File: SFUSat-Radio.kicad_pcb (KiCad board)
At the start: 2 copper layers, 95.9 x 90.2 mm, 84 parts, among them J1 PC104-8BIT, J2 PC104PTH, J3 PC104PTH, J4 PC104PTH, J5 PC104PTH, J6 SMA, J7 SMA, J8 SMA, J9 SMA, P1 CONN_02X05, P2 CONN_01X03, P3 CONN_01X03, P4 CONN_01X03, U1 2N7002DW, U10 RT9183, U2 CC1101-Q1, U3 0433BM15A0001, U4 SINGLE_0402, U5 SKY13372-467LF, U6 SINGLE_0402, U7 SINGLE_0402, U8 SKY65366-21, U9 TPS799, X1 NX3225GA

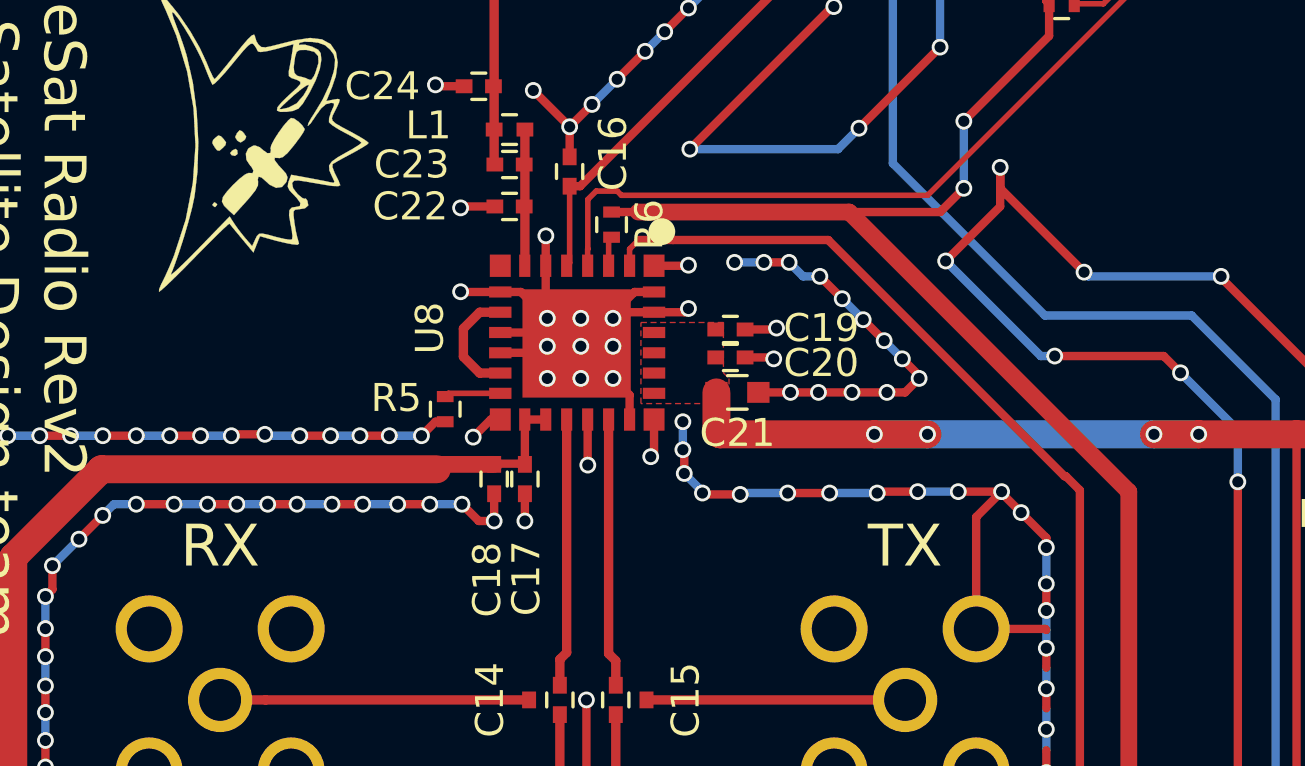
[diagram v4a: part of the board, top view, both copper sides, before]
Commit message: IC->passive pad 30mil clearance
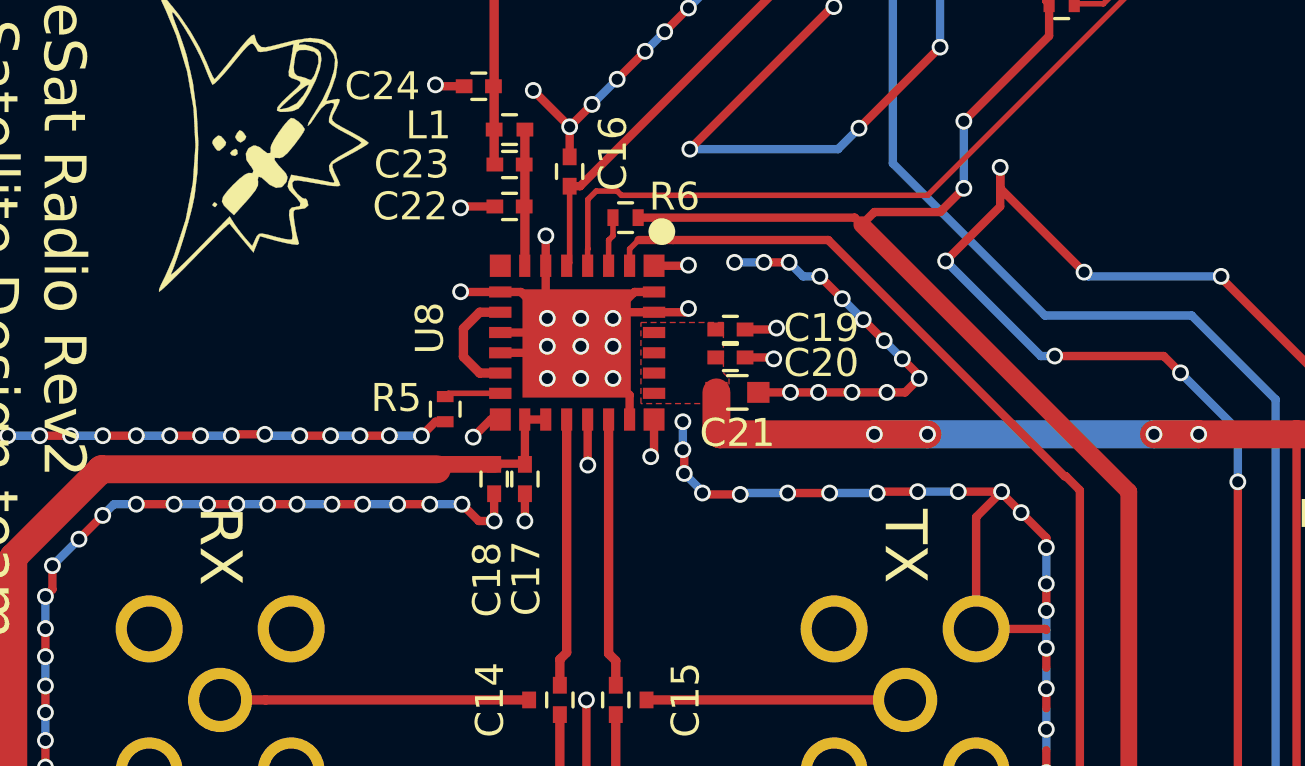
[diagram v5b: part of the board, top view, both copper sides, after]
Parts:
- moved R6 0.56 mm to (140.5, 85.8), turned to 180 degrees
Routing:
- net /VDD_3.3: track 299.1 -> 297.9 mm
- net Net-(R6-Pad2): track 1.06 -> 1.78 mm
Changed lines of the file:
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@@
     (thickness 1.6)
     (drawings 27)
-    (tracks 1250)
+    (tracks 1252)
     (zones 0)
     (modules 84)
@@
   )
   (module SFUSat:R_0402 (layer F.Cu)
-    (at 140 86 270)
+    (at 140.5 85.75 180)
     (descr "Resistor SMD 0402, reflow soldering, Vishay (see dcrcw.pdf)")
     (tags "resistor 0402")
     (attr smd)
-    (fp_text reference R6 (at 0 -1.35 270) (layer F.SilkS)
+    (fp_text reference R6 (at -1.75 0.75 180) (layer F.SilkS)
       (effects (font (size 1 1) (thickness 0.15)))
     )
-    (fp_text value 1k (at 0 1.45 270) (layer F.Fab)
+    (fp_text value 1k (at 0 1.45 180) (layer F.Fab)
       (effects (font (size 1 1) (thickness 0.15)))
     )
-    (fp_text user %R (at 0 -1.35 270) (layer F.Fab)
+    (fp_text user %R (at 0 -1.35 180) (layer F.Fab)
       (effects (font (size 1 1) (thickness 0.15)))
     )
@@
     (fp_line (start 0.8 0.45) (end 0.8 -0.45) (layer F.CrtYd) (width 0.05))
     (fp_line (start 0.8 0.45) (end -0.8 0.45) (layer F.CrtYd) (width 0.05))
-    (pad 1 smd rect (at -0.45 0 270) (size 0.4 0.6) (layers F.Cu F.Paste F.Mask)
+    (pad 1 smd rect (at -0.45 0 180) (size 0.4 0.6) (layers F.Cu F.Paste F.Mask)
       (net 4 /VDD_3.3) (solder_paste_margin -0.02))
-    (pad 2 smd rect (at 0.45 0 270) (size 0.4 0.6) (layers F.Cu F.Paste F.Mask)
+    (pad 2 smd rect (at 0.45 0 180) (size 0.4 0.6) (layers F.Cu F.Paste F.Mask)
       (net 89 "Net-(R6-Pad2)") (solder_paste_margin -0.02))
     (model Resistors_SMD.3dshapes/R_0402.wrl
@@
     (effects (font (size 1.5 1.5) (thickness 0.3)))
   )
-  (gr_text TX (at 150.5 97.5) (layer F.SilkS)
+  (gr_text TX (at 150.5 97.5 270) (layer F.SilkS)
     (effects (font (size 1.5 1.5) (thickness 0.3)))
   )
-  (gr_text RX (at 126 97.5) (layer F.SilkS)
+  (gr_text RX (at 126 97.5 270) (layer F.SilkS)
     (effects (font (size 1.5 1.5) (thickness 0.3)))
   )
@@
   (segment (start 150 126.95) (end 150 125.45) (width 0.2) (layer F.Cu) (net 3))
   (segment (start 150 125.45) (end 149.95 125.4) (width 0.2) (layer F.Cu) (net 3))
+  (segment (start 151.75 85.55) (end 149.398542 85.55) (width 0.3) (layer F.Cu) (net 4))
+  (segment (start 149.398542 85.55) (end 148.948542 86) (width 0.3) (layer F.Cu) (net 4))
+  (segment (start 148.948542 86) (end 158.5 95.551458) (width 0.6) (layer F.Cu) (net 4))
+  (segment (start 148.698542 85.75) (end 148.948542 86) (width 0.3) (layer F.Cu) (net 4))
+  (segment (start 140.95 85.75) (end 148.698542 85.75) (width 0.3) (layer F.Cu) (net 4))
   (segment (start 176.399999 146.100001) (end 170.35 146.100001) (width 0.3) (layer F.Cu) (net 4))
   (segment (start 170.35 146.100001) (end 168.9 146.100001) (width 0.3) (layer F.Cu) (net 4))
@@
   (via (at 152.6 82.3) (size 0.6) (drill 0.4) (layers F.Cu B.Cu) (net 4))
   (segment (start 152.6 84.7) (end 152.6 82.3) (width 0.3) (layer B.Cu) (net 4))
-  (segment (start 148.498542 85.55) (end 151.75 85.55) (width 0.3) (layer F.Cu) (net 4))
   (segment (start 151.75 85.55) (end 152.6 84.7) (width 0.3) (layer F.Cu) (net 4))
   (via (at 152.6 84.7) (size 0.6) (drill 0.4) (layers F.Cu B.Cu) (net 4))
@@
   (segment (start 158.5 125.948542) (end 158.5 115.8) (width 0.6) (layer F.Cu) (net 4))
   (segment (start 158.5 115.8) (end 158.5 116.2) (width 0.6) (layer F.Cu) (net 4))
-  (segment (start 140.95 85.55) (end 148.498542 85.55) (width 0.6) (layer F.Cu) (net 4))
-  (segment (start 148.498542 85.55) (end 158.5 95.551458) (width 0.6) (layer F.Cu) (net 4))
   (segment (start 145.15 127.4) (end 145.15 127.45) (width 0.3) (layer F.Cu) (net 4))
   (segment (start 143.7 125.25) (end 143.7 125.36261) (width 0.3) (layer F.Cu) (net 4))
@@
   (segment (start 136.9 94.55) (end 136.9 92.976) (width 0.3) (layer F.Cu) (net 4))
   (segment (start 136.9 92.976) (end 136.8945 92.9705) (width 0.3) (layer F.Cu) (net 4))
-  (segment (start 140 85.55) (end 140.95 85.55) (width 0.3) (layer F.Cu) (net 4))
   (segment (start 142.875 130) (end 144.288001 129.999999) (width 0.2) (layer F.Cu) (net 5))
   (segment (start 144.288001 129.999999) (end 144.600001 130.311999) (width 0.2) (layer F.Cu) (net 5))
@@
   (segment (start 136.0195 92.0335) (end 134.1665 92.0335) (width 0.2) (layer F.Cu) (net 88))
   (segment (start 134.1665 92.0335) (end 134.05 92.15) (width 0.2) (layer F.Cu) (net 88))
-  (segment (start 139.8945 87.4705) (end 139.8945 86.5555) (width 0.2) (layer F.Cu) (net 89))
-  (segment (start 139.8945 86.5555) (end 140 86.45) (width 0.2) (layer F.Cu) (net 89))
+  (segment (start 140.05 85.75) (end 140.05 86.4) (width 0.2) (layer F.Cu) (net 89))
+  (segment (start 140.05 86.4) (end 139.8945 86.5555) (width 0.2) (layer F.Cu) (net 89))
+  (segment (start 139.8945 86.5555) (end 139.8945 87.4705) (width 0.2) (layer F.Cu) (net 89))
   (segment (start 176.566726 96.321568) (end 176.566726 99.324568) (width 0.2) (layer F.Cu) (net 90))
   (segment (start 176.566726 99.324568) (end 177.009726 99.767568) (width 0.2) (layer F.Cu) (net 90))

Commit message: generated gerbers
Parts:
- removed C18: 220pF, SFUSat:C_0402
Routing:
- net GND: track 682.4 -> 655.8 mm, vias 288 -> 266
- net (no net): track 22.2 -> 47.7 mm, vias 15 -> 42

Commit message: added PCBway info
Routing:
- net (no net): track 47.7 -> 0.00 mm, vias 42 -> 0
- net GND: track 655.8 -> 699.4 mm, vias 266 -> 316
- net Net-(C22-Pad1): track 4.88 -> 5.90 mm
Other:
- net class RF: trace_width 0.335589 -> 1.05758

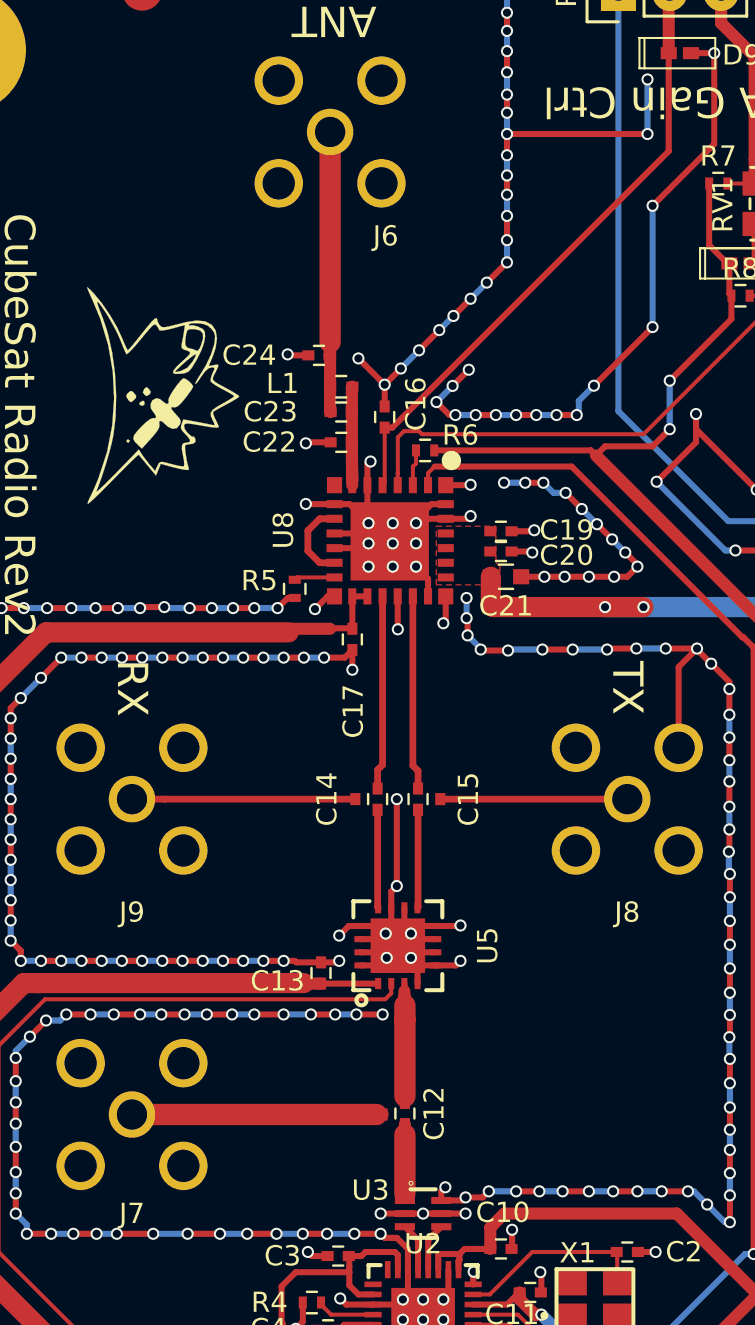
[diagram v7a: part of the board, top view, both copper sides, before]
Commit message: fixed microstrip
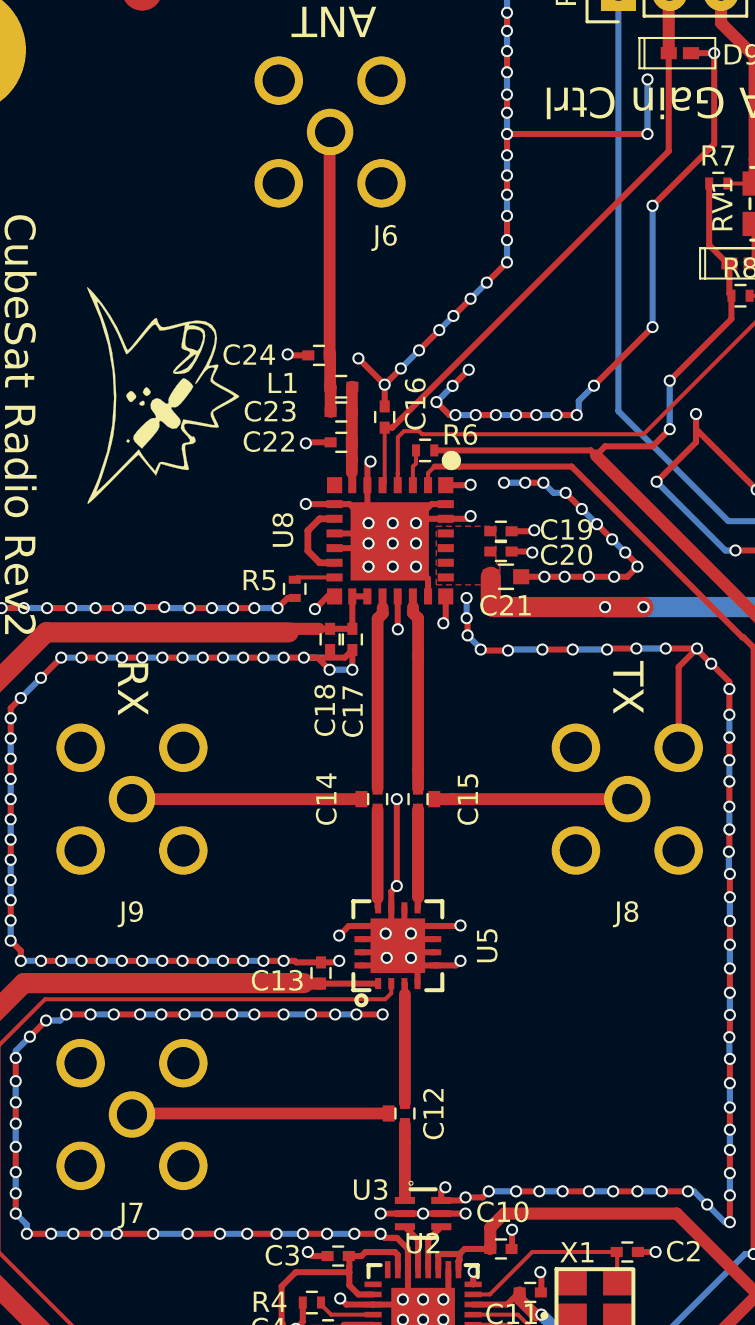
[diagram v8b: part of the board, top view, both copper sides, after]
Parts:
- added C18: 220pF, SFUSat:C_0402, F.Cu at (135.8, 95.1)
- moved U4 0.30 mm to (138.7, 118.5), turned to 90 degrees
- moved U7 0.30 mm to (140.9, 103.0), turned to 270 degrees
- moved U6 0.30 mm to (137.3, 103.0), turned to 90 degrees
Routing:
- net GND: track 699.4 -> 702.0 mm
- net Net-(C22-Pad1): track 5.90 -> 4.89 mm
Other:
- net class RF: trace_width 1.05758 -> 0.585982
